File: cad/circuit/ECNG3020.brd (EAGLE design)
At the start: 80 x 60.6 mm, 23 parts, among them Q1 16Mhz, U1 ATMEGA328P-PU

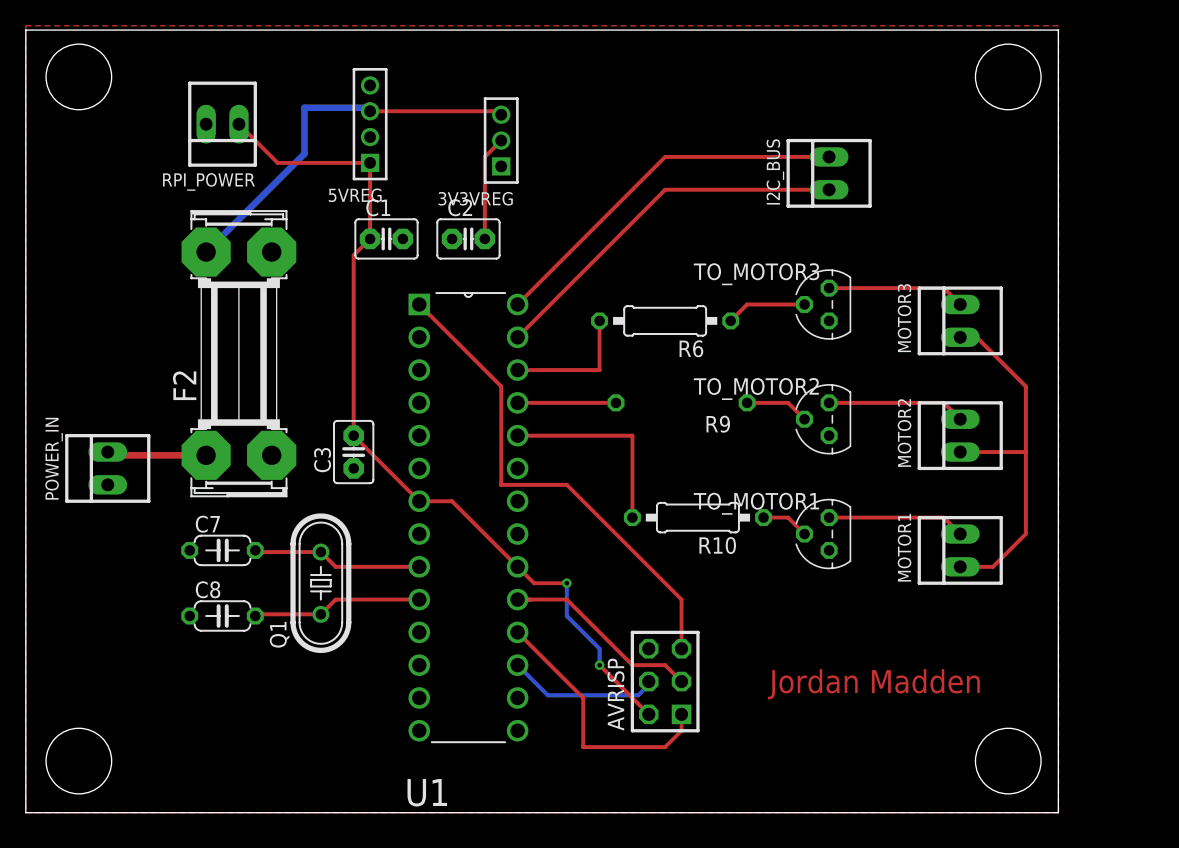
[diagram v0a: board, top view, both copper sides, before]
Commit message: Put 2 5V bucks in parallel to increase current to rpi
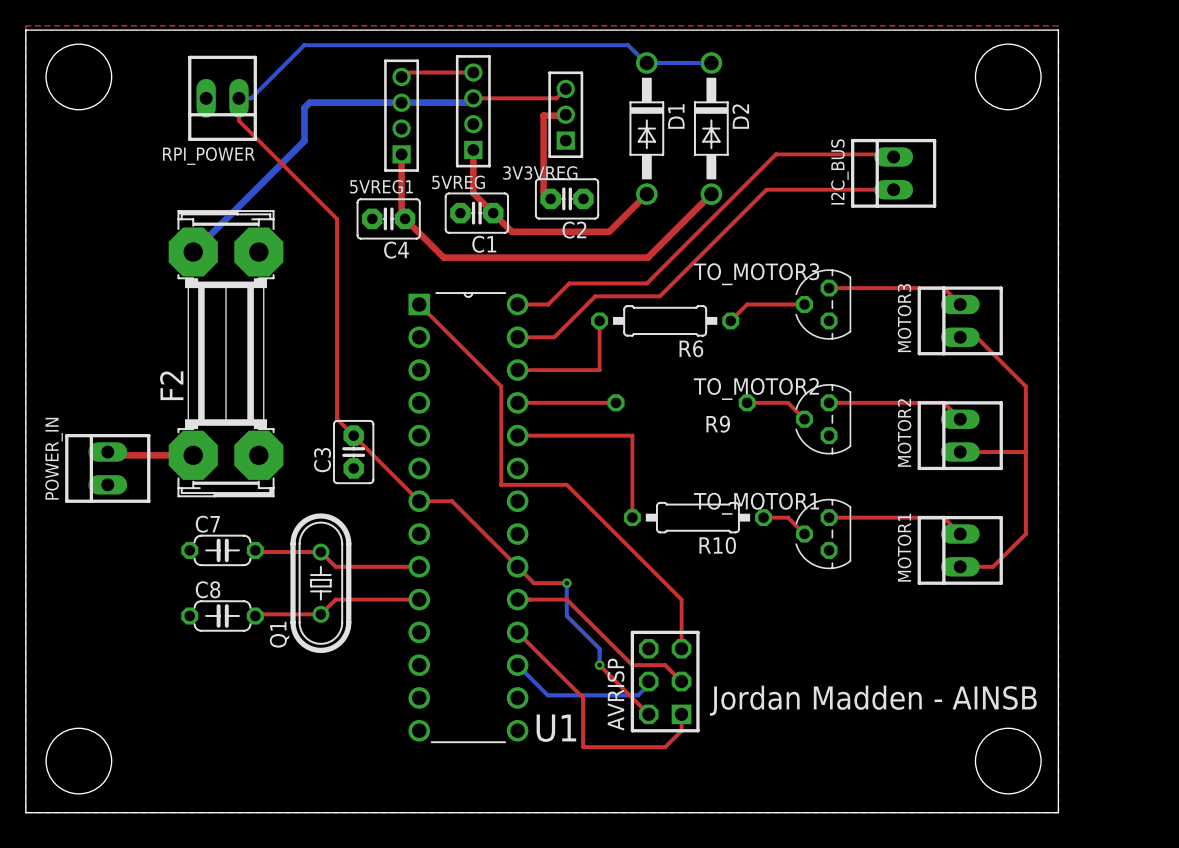
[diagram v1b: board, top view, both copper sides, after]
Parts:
- added 5VREG1: (no value), pinhead_2:1X04M
- added C4: (no value), capacitor-wima:C2.5-3
- added D1, D2: 1N4004, diode:DO41-10
- moved C2 8.24 mm to (50.8, 47.5), turned to 180 degrees
- moved 5VREG 8.06 mm to (43.6, 54.3)
- moved C1 7.28 mm to (43.8, 46.5), turned to 180 degrees
- moved 3V3VREG 5.39 mm to (50.7, 54.1)
- moved I2C_BUS 5.00 mm to (76.1, 49.5)
- moved RPI_POWER 2.00 mm to (24.1, 55.3)
- moved F2 1.00 mm to (24.4, 35.6)
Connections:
- new net VCC_A: 5VREG.1, C1.1, D1.A
- new net VCC_B: 5VREG1.1, C4.1, D2.A
- net 12V: now also 5VREG1.3
- net EN: now also 5VREG1.4
- net GND: now also 5VREG1.2, C4.2
- net VCC: now also D1.C, D2.C; no longer 5VREG.1, C1.1
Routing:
- net VCC: track 67.1 -> 102.7 mm
- net VCC_B: track 0.00 -> 32.1 mm
- net VCC_A: track 0.00 -> 19.2 mm
- net 12V: track 29.8 -> 36.0 mm
- net EN: track 0.00 -> 5.70 mm
- net SCL: track 28.9 -> 34.0 mm
- net SDA: track 28.9 -> 33.9 mm
- net N$13: track 7.73 -> 6.73 mm
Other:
- board text added: "Jordan Madden - AINSB"
- board text removed: "Jordan Madden"

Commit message: Re-routed some connections
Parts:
- moved RPI_POWER 3.61 mm to (21.1, 53.3)
- moved R6 3.00 mm to (61.4, 38.1)
- moved 5VREG1 2.00 mm to (36.0, 54.0)
- moved TO_MOTOR3 1.41 mm to (72.1, 38.4)
- moved C4 1.00 mm to (36.0, 46.0)
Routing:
- net VCC: track 102.7 -> 106.6 mm, vias 2 -> 3
- net N$4: track 10.2 -> 13.2 mm
- net N$15: track 6.24 -> 3.83 mm
- net EN: track 5.70 -> 7.70 mm
- net N$10: track 10.7 -> 9.27 mm
- net VCC_B: track 32.1 -> 33.5 mm

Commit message: Corrected 3.3V connection on PCB
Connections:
- removed net N$7: MOTOR1.1, MOTOR2.1, MOTOR3.1
- net 3.3: now also MOTOR1.1, MOTOR2.1, MOTOR3.1
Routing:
- net 3.3: track 8.43 -> 73.9 mm
- net N$7: track 29.3 -> 0.00 mm
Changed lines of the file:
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@@
 <wire x1="49" y1="54" x2="49" y2="48.1" width="0.508" layer="1"/>
 <wire x1="49" y1="48.1" x2="49.55" y2="47.55" width="0.508" layer="1"/>
+<contactref element="MOTOR2" pad="1"/>
+<contactref element="MOTOR1" pad="1"/>
+<contactref element="MOTOR3" pad="1"/>
+<wire x1="81.28" y1="36.83" x2="82.55" y2="36.83" width="0.3048" layer="1"/>
+<wire x1="82.55" y1="36.83" x2="86.36" y2="33.02" width="0.3048" layer="1"/>
+<wire x1="86.36" y1="33.02" x2="86.36" y2="27.94" width="0.3048" layer="1"/>
+<wire x1="86.36" y1="27.94" x2="86.36" y2="21.59" width="0.3048" layer="1"/>
+<wire x1="86.36" y1="21.59" x2="83.82" y2="19.05" width="0.3048" layer="1"/>
+<wire x1="83.82" y1="19.05" x2="81.28" y2="19.05" width="0.3048" layer="1"/>
+<wire x1="81.28" y1="27.94" x2="86.36" y2="27.94" width="0.3048" layer="1"/>
+<wire x1="49.55" y1="47.55" x2="55.1" y2="42" width="0.3048" layer="16"/>
+<wire x1="76.11" y1="42" x2="81.28" y2="36.83" width="0.3048" layer="16"/>
+<wire x1="55.1" y1="42" x2="76.11" y2="42" width="0.3048" layer="16"/>
 </signal>
 <signal name="EN">
@@
 <wire x1="58.42" y1="11.43" x2="59.69" y2="10.16" width="0.3048" layer="1"/>
 </signal>
-<signal name="N$7">
-<contactref element="MOTOR2" pad="1"/>
-<contactref element="MOTOR1" pad="1"/>
-<contactref element="MOTOR3" pad="1"/>
-<wire x1="81.28" y1="36.83" x2="82.55" y2="36.83" width="0.3048" layer="1"/>
-<wire x1="82.55" y1="36.83" x2="86.36" y2="33.02" width="0.3048" layer="1"/>
-<wire x1="86.36" y1="33.02" x2="86.36" y2="27.94" width="0.3048" layer="1"/>
-<wire x1="86.36" y1="27.94" x2="86.36" y2="21.59" width="0.3048" layer="1"/>
-<wire x1="86.36" y1="21.59" x2="83.82" y2="19.05" width="0.3048" layer="1"/>
-<wire x1="83.82" y1="19.05" x2="81.28" y2="19.05" width="0.3048" layer="1"/>
-<wire x1="81.28" y1="27.94" x2="86.36" y2="27.94" width="0.3048" layer="1"/>
-</signal>
 <signal name="SDA">
